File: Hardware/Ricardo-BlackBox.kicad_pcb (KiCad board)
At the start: 4 copper layers, 45.1 x 35.1 mm, 83 parts, among them J1 RBUS, J2 USB_C_Receptacle_USB2.0, J3 Conn_01x08_Pin, U1 ESP32-S3, U2 SN65HVD230, U3 LM66200DRLR, U4 MAX77827AEFD+T, U5 SC4215ASTRT, U7 LM66200DRLR, Y1 R940000171

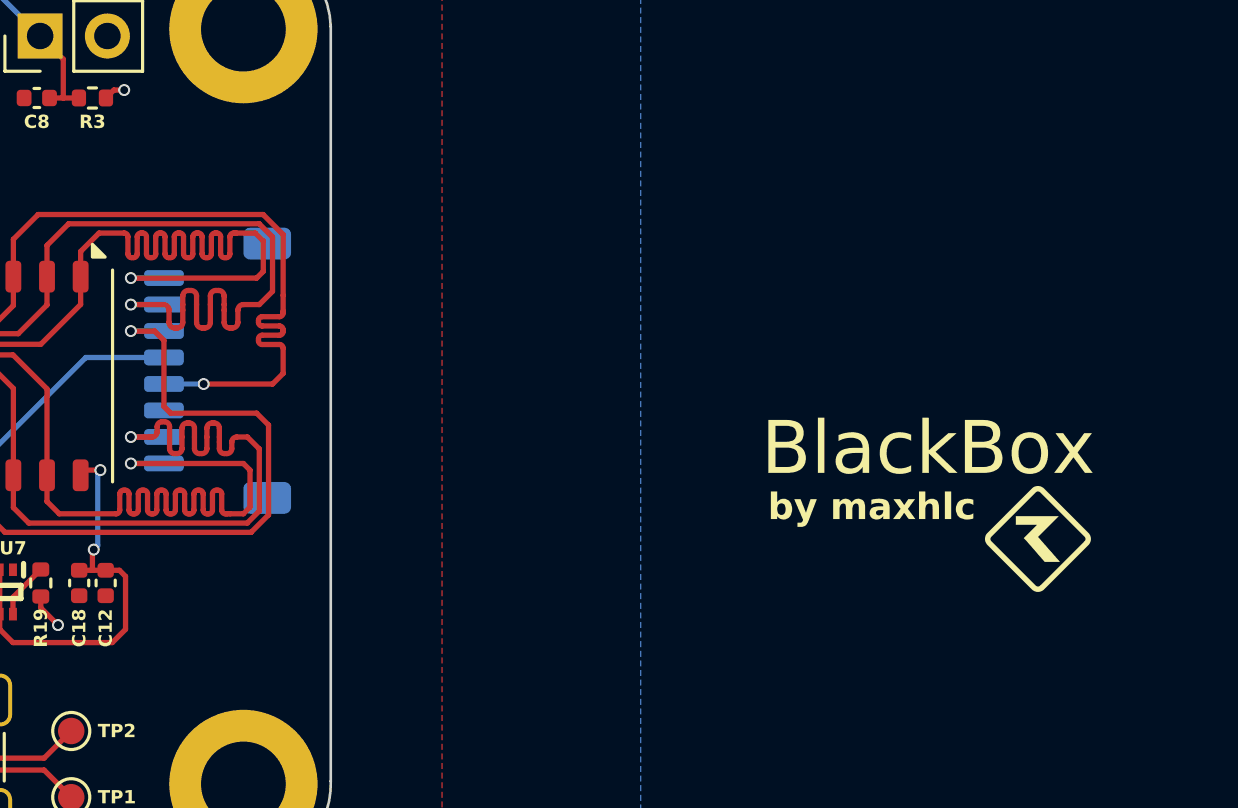
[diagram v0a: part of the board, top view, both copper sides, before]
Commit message: Update name position
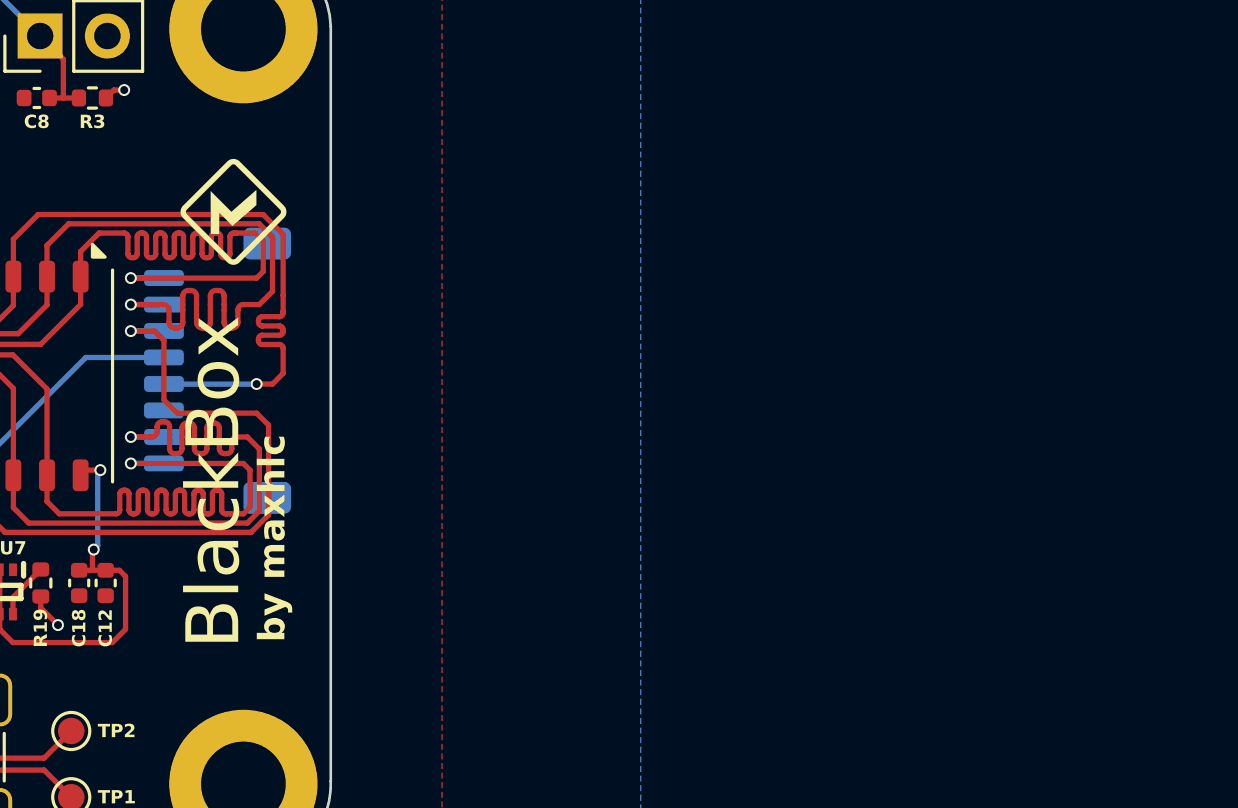
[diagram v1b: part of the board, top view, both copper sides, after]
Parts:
- moved G*** 32.8 mm to (120.5, 56.0), turned to 90 degrees
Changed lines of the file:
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@@
 	(footprint "iclr:rae_logo_4mm"
 		(layer "F.Cu")
-		(at 150.925 68.34)
+		(at 120.549953 55.989857 90)
 		(property "Reference" "G***"
-			(at 0 0 0)
+			(at 0 0 90)
 			(layer "F.SilkS")
 			(hide yes)
@@
 		)
 		(property "Value" "LOGO"
-			(at 0.75 0 0)
+			(at 0.75 0 90)
 			(layer "F.SilkS")
 			(hide yes)
@@
 		)
 		(property "Footprint" "iclr:rae_logo_4mm"
-			(at 0 0 0)
+			(at 0 0 90)
 			(unlocked yes)
 			(layer "F.Fab")
@@
 		)
 		(property "Datasheet" ""
-			(at 0 0 0)
+			(at 0 0 90)
 			(unlocked yes)
 			(layer "F.Fab")
@@
 		)
 		(property "Description" ""
-			(at 0 0 0)
+			(at 0 0 90)
 			(unlocked yes)
 			(layer "F.Fab")
@@
 	)
 	(gr_text "BlackBox"
-		(at 140.475 66.09 0)
+		(at 120.975 72.489857 90)
 		(layer "F.SilkS")
 		(effects
@@
 	)
 	(gr_text "by maxhlc"
-		(at 140.725 66.54 0)
+		(at 121.425 72.239857 90)
 		(layer "F.SilkS")
 		(effects
@@
 	)
 	(segment
-		(start 122.425 62.09)
-		(end 122.425 61.137574)
-		(width 0.2)
-		(layer "F.Cu")
-		(net 67)
-	)
-	(segment
 		(start 113.175 56.09)
 		(end 112.24 57.025)
@@
 	)
 	(segment
-		(start 121.669974 56.09)
-		(end 113.175 56.09)
+		(start 121.425 62.49)
+		(end 122.025 62.49)
 		(width 0.2)
 		(layer "F.Cu")
@@
 	)
 	(segment
-		(start 122.025 62.49)
-		(end 122.425 62.09)
+		(start 121.669974 56.09)
+		(end 113.175 56.09)
 		(width 0.2)
 		(layer "F.Cu")
@@
 	)
 	(segment
-		(start 119.425 62.49)
-		(end 122.025 62.49)
+		(start 122.025 62.49)
+		(end 122.425 62.09)
 		(width 0.2)
 		(layer "F.Cu")
@@
 	)
 	(segment
+		(start 122.425 62.09)
+		(end 122.425 61.137574)
+		(width 0.2)
+		(layer "F.Cu")
+		(net 67)
+	)
+	(segment
 		(start 122.425 60.507574)
 		(end 122.425 60.437574)
@@
 	)
 	(via
-		(at 119.425 62.49)
+		(at 121.425 62.49)
 		(size 0.45)
 		(drill 0.3)
@@
 	)
 	(segment
-		(start 117.9275 62.49)
-		(end 117.925 62.4875)
+		(start 121.425 62.49)
+		(end 117.9275 62.49)
 		(width 0.2)
 		(layer "B.Cu")
@@
 	)
 	(segment
-		(start 119.425 62.49)
-		(end 117.9275 62.49)
+		(start 117.9275 62.49)
+		(end 117.925 62.4875)
 		(width 0.2)
 		(layer "B.Cu")
@@
 	)
 	(segment
-		(start 110.525 62.19)
-		(end 108.17 62.19)
+		(start 121.875 64.04)
+		(end 121.425 63.59)
 		(width 0.2)
 		(layer "F.Cu")
@@
 	)
 	(segment
-		(start 121.875 67.42995)
-		(end 121.875 64.04)
+		(start 110.525 62.19)
+		(end 108.17 62.19)
 		(width 0.2)
 		(layer "F.Cu")
@@
 	)
 	(segment
-		(start 121.875 64.04)
-		(end 121.425 63.59)
+		(start 117.925 60.845025)
+		(end 117.569975 60.49)
 		(width 0.2)
 		(layer "F.Cu")
@@
 	)
 	(segment
-		(start 121.425 63.59)
-		(end 118.175 63.59)
+		(start 117.925 63.09)
+		(end 117.925 60.845025)
 		(width 0.2)
 		(layer "F.Cu")
@@
 	)
 	(segment
-		(start 117.925 63.34)
-		(end 117.925 60.845025)
+		(start 121.875 67.42995)
+		(end 121.875 64.04)
 		(width 0.2)
 		(layer "F.Cu")
@@
 	)
 	(segment
-		(start 111.925 68.09)
-		(end 121.21495 68.09)
+		(start 118.425 63.59)
+		(end 117.925 63.09)
 		(width 0.2)
 		(layer "F.Cu")
@@
 	)
 	(segment
-		(start 110.97 65.935)
-		(end 110.97 67.135)
+		(start 121.21495 68.09)
+		(end 121.875 67.42995)
 		(width 0.2)
 		(layer "F.Cu")
@@
 	)
 	(segment
-		(start 118.175 63.59)
-		(end 117.925 63.34)
+		(start 110.97 65.935)
+		(end 110.97 67.135)
 		(width 0.2)
 		(layer "F.Cu")
@@
 	)
 	(segment
-		(start 117.925 60.845025)
-		(end 117.569975 60.49)
+		(start 110.97 67.135)
+		(end 111.925 68.09)
 		(width 0.2)
 		(layer "F.Cu")
@@
 	)
 	(segment
-		(start 121.21495 68.09)
-		(end 121.875 67.42995)
+		(start 121.425 63.59)
+		(end 118.425 63.59)
 		(width 0.2)
 		(layer "F.Cu")
@@
 	)
 	(segment
-		(start 110.97 65.935)
-		(end 110.97 62.635)
+		(start 111.925 68.09)
+		(end 121.21495 68.09)
 		(width 0.2)
 		(layer "F.Cu")
@@
 	)
 	(segment
-		(start 110.97 67.135)
-		(end 111.925 68.09)
+		(start 110.97 65.935)
+		(end 110.97 62.635)
 		(width 0.2)
 		(layer "F.Cu")
@@
 	)
 	(zone
+		(net 1)
+		(net_name "GND")
+		(layer "F.Cu")
+		(name "$teardrop_padvia$")
+		(hatch full 0.1)
+		(priority 30003)
+		(attr
+			(teardrop
+				(type padvia)
+			)
+		)
+		(connect_pads yes
+			(clearance 0)
+		)
+		(min_thickness 0.0254)
+		(filled_areas_thickness no)
+		(fill yes
+			(thermal_gap 0.5)
+			(thermal_bridge_width 0.5)
+			(island_removal_mode 1)
+			(island_area_min 10)
+		)
+		(polygon
+			(pts
+				(xy 97.053482 69.861882) (xy 97.053482 69.661882) (xy 96.645784 69.864009) (xy 96.730888 70.071882)
+				(xy 96.939761 70.157986)
+			)
+		)
+	)
+	(zone
+		(net 3)
+		(net_name "VBUS")
+		(layer "F.Cu")
+		(name "$teardrop_padvia$")
+		(hatch full 0.1)
+		(priority 30000)
+		(attr
+			(teardrop
+				(type padvia)
+			)
+		)
+		(connect_pads yes
+			(clearance 0)
+		)
+		(min_thickness 0.0254)
+		(filled_areas_thickness no)
+		(fill yes
+			(thermal_gap 0.5)
+			(thermal_bridge_width 0.5)
+			(island_removal_mode 1)
+			(island_area_min 10)
+		)
+		(polygon
+			(pts
+				(xy 88.322458 76.138882) (xy 88.322458 75.888882) (xy 87.992992 75.694009) (xy 87.905888 75.901882)
+				(xy 87.906888 76.126882)
+			)
+		)
+	)
+	(zone
 		(net 2)
 		(net_name "+3V3")
@@
 	)
 	(zone
-		(net 3)
-		(net_name "VBUS")
+		(net 1)
+		(net_name "GND")
 		(layer "F.Cu")
 		(name "$teardrop_padvia$")
 		(hatch full 0.1)
-		(priority 30002)
+		(priority 30001)
 		(attr
 			(teardrop
@@
 		(polygon
 			(pts
-				(xy 87.316888 72.236441) (xy 87.566888 72.236441) (xy 87.843071 72.045814) (xy 87.683972 71.885715)
-				(xy 87.476099 71.800611)
+				(xy 88.316888 72.386882) (xy 88.566888 72.386882) (xy 88.649761 72.022986) (xy 88.441888 71.935882)
+				(xy 88.234015 72.022986)
 			)
 		)
@@
 	)
 	(zone
-		(net 1)
-		(net_name "GND")
-		(layer "F.Cu")
-		(name "$teardrop_padvia$")
-		(hatch full 0.1)
-		(priority 30001)
-		(attr
-			(teardrop
-				(type padvia)
-			)
-		)
-		(connect_pads yes
-			(clearance 0)
-		)
-		(min_thickness 0.0254)
-		(filled_areas_thickness no)
-		(fill yes
-			(thermal_gap 0.5)
-			(thermal_bridge_width 0.5)
-			(island_removal_mode 1)
-			(island_area_min 10)
-		)
-		(polygon
-			(pts
-				(xy 88.316888 72.386882) (xy 88.566888 72.386882) (xy 88.649761 72.022986) (xy 88.441888 71.935882)
-				(xy 88.234015 72.022986)
-			)
-		)
-	)
-	(zone
-		(net 1)
-		(net_name "GND")
-		(layer "F.Cu")
-		(name "$teardrop_padvia$")
-		(hatch full 0.1)
-		(priority 30003)
-		(attr
-			(teardrop
-				(type padvia)
-			)
-		)
-		(connect_pads yes
-			(clearance 0)
-		)
-		(min_thickness 0.0254)
-		(filled_areas_thickness no)
-		(fill yes
-			(thermal_gap 0.5)
-			(thermal_bridge_width 0.5)
-			(island_removal_mode 1)
-			(island_area_min 10)
-		)
-		(polygon
-			(pts
-				(xy 97.053482 69.861882) (xy 97.053482 69.661882) (xy 96.645784 69.864009) (xy 96.730888 70.071882)
-				(xy 96.939761 70.157986)
-			)
-		)
-	)
-	(zone
 		(net 8)
 		(net_name "/Power/LX1")
@@
 		(name "$teardrop_padvia$")
 		(hatch full 0.1)
-		(priority 30000)
+		(priority 30002)
 		(attr
 			(teardrop
@@
 		(polygon
 			(pts
-				(xy 88.322458 76.138882) (xy 88.322458 75.888882) (xy 87.992992 75.694009) (xy 87.905888 75.901882)
-				(xy 87.906888 76.126882)
+				(xy 87.316888 72.236441) (xy 87.566888 72.236441) (xy 87.843071 72.045814) (xy 87.683972 71.885715)
+				(xy 87.476099 71.800611)
 			)
 		)
@@
 		(name "$teardrop_padvia$")
 		(hatch full 0.1)
-		(priority 30000)
+		(priority 30002)
 		(attr
 			(teardrop
@@
 		(polygon
 			(pts
-				(xy 88.090558 71.656906) (xy 87.913781 71.480129) (xy 87.597868 71.678842) (xy 87.683265 71.887422)
-				(xy 87.891845 71.972819)
+				(xy 87.776888 72.246452) (xy 88.026888 72.246452) (xy 87.891845 71.800611) (xy 87.683972 71.885715)
+				(xy 87.524873 72.045814)
 			)
 		)
@@
 		(name "$teardrop_padvia$")
 		(hatch full 0.1)
-		(priority 30002)
+		(priority 30000)
 		(attr
 			(teardrop
@@
 		(polygon
 			(pts
-				(xy 87.776888 72.246452) (xy 88.026888 72.246452) (xy 87.891845 71.800611) (xy 87.683972 71.885715)
-				(xy 87.524873 72.045814)
+				(xy 88.090558 71.656906) (xy 87.913781 71.480129) (xy 87.597868 71.678842) (xy 87.683265 71.887422)
+				(xy 87.891845 71.972819)
 			)
 		)

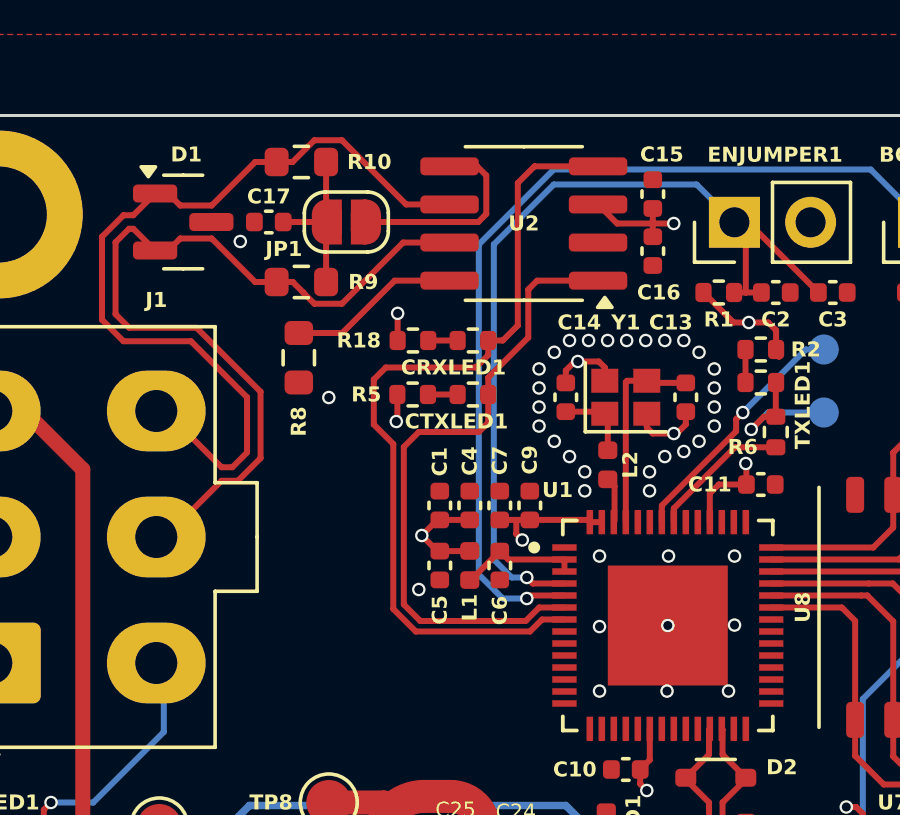
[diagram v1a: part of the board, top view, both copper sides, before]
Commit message: Moved CAN RX/TX lines
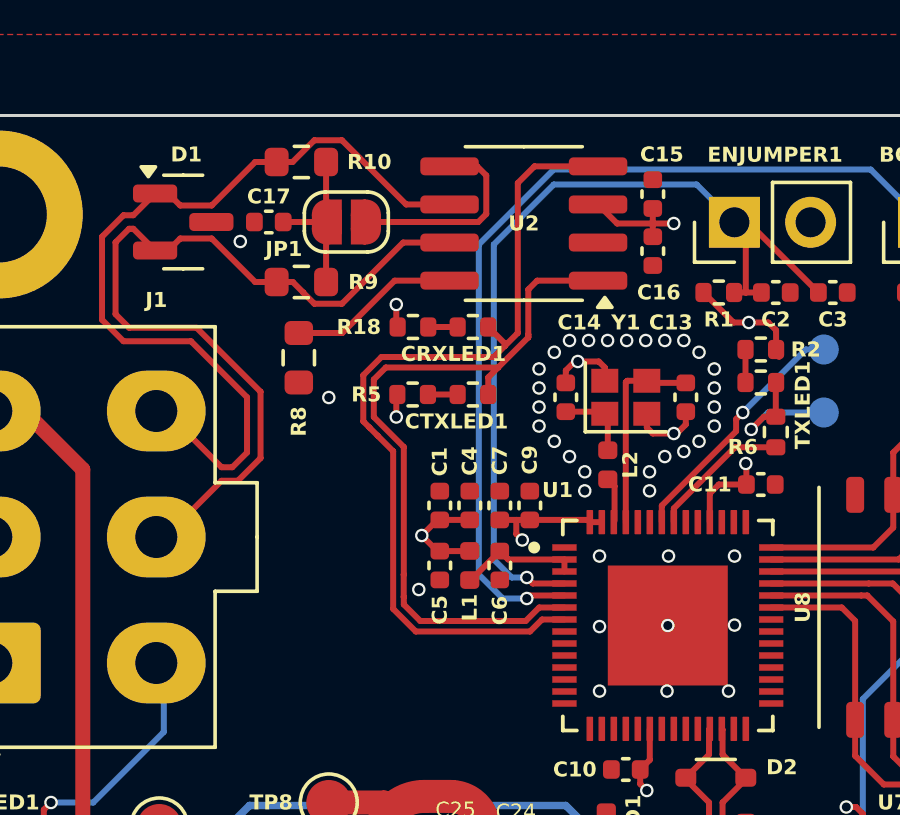
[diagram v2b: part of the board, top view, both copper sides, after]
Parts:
- moved CRXLED1 0.45 mm to (98.2, 52.8)
- moved R18 0.45 mm to (96.2, 52.8)
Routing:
- net /CAN_TX: track 21.6 -> 24.6 mm
- net /CAN_RX: track 27.9 -> 29.2 mm
